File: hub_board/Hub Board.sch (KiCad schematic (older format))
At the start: 26 parts, among them J1 DotStar, J2 DotStar, J3 DotStar, J4 DotStar, J5 Sensor, P4 SERIAL, SW1 Switch_SPDT_x2, SW2 Switch_DPST, U0 10118194, U1 LM3671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

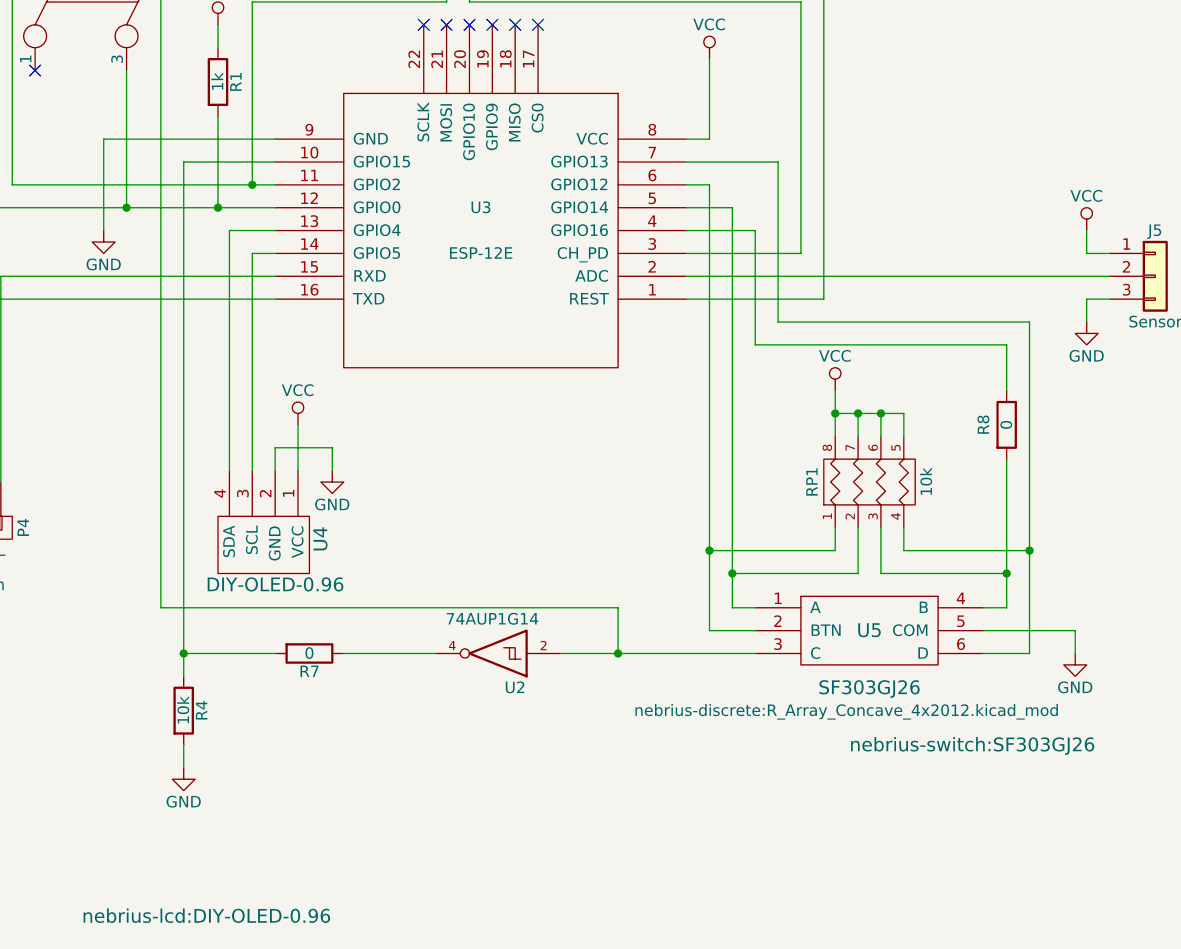
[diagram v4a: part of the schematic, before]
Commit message: Removed jumpers
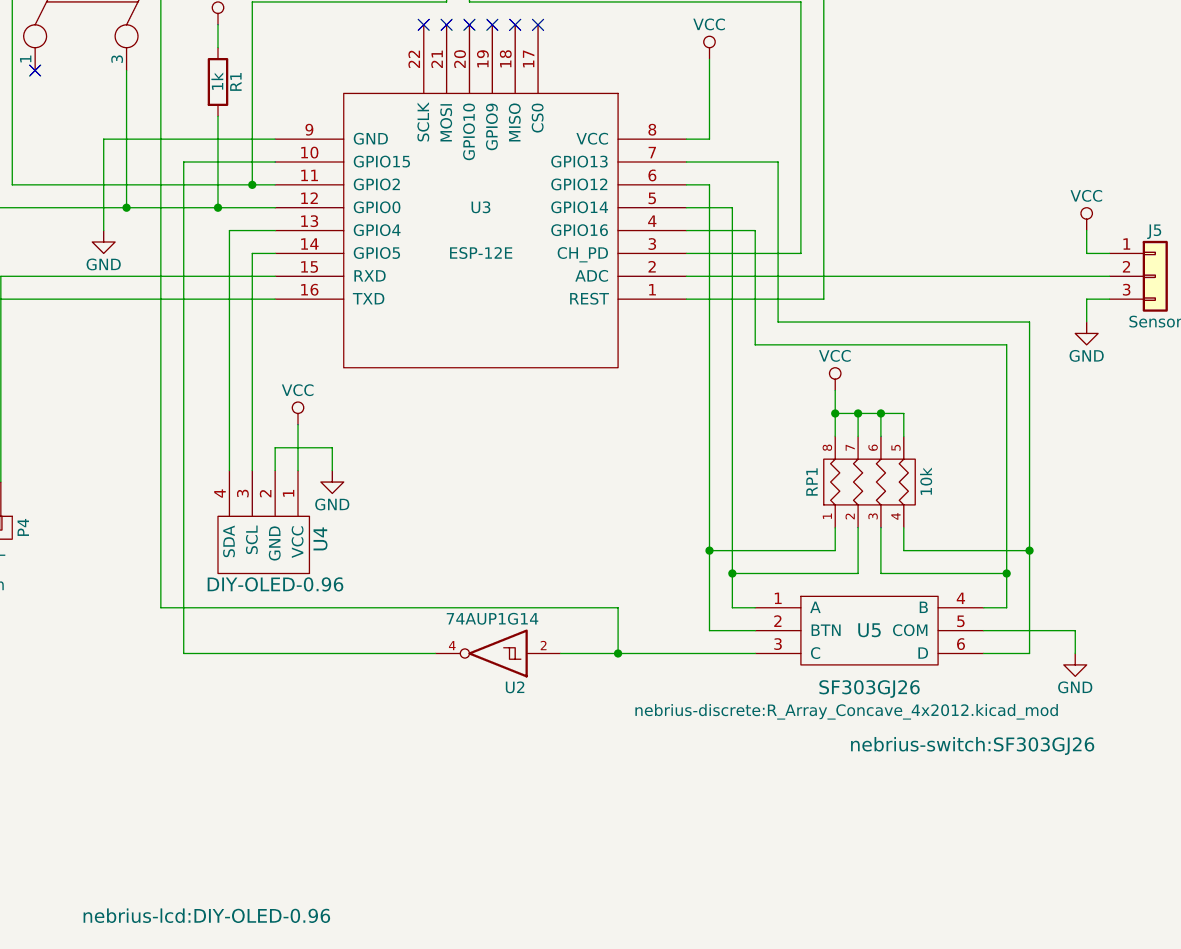
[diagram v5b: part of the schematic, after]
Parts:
- removed R4: 10k, Resistors_SMD:R_0805_HandSoldering, symbol R
- removed R7, R8: 0, Resistors_SMD:R_0805_HandSoldering, symbol R
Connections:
- net at U3.10 (GPIO15): now also U2.4
- net at U3.4 (GPIO16): now also RP1.3 (P3), U5.4 (B)
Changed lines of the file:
@@
 	9250 6400 9250 6500
-Wire Wire Line
-	5350 4350 5350 6600
 Wire Wire Line
 	7250 6300 7250 6500
@@
 	-1   0    0    1
 $EndComp
-$Comp
-L R R4
-U 1 1 5AB19A67
-P 5350 6750
-F 0 "R4" V 5430 6750 50  0000 C CNN
-F 1 "10k" V 5350 6750 50  0000 C CNN
-F 2 "Resistors_SMD:R_0805_HandSoldering" V 5280 6750 50  0001 C CNN
-F 3 "" H 5350 6750 50  0001 C CNN
-	1    5350 6750
-	1    0    0    -1
-$EndComp
-$Comp
-L R R7
-U 1 1 5AB19B14
-P 5900 6500
-F 0 "R7" V 5980 6500 50  0000 C CNN
-F 1 "0" V 5900 6500 50  0000 C CNN
-F 2 "Resistors_SMD:R_0805_HandSoldering" V 5830 6500 50  0001 C CNN
-F 3 "" H 5900 6500 50  0001 C CNN
-	1    5900 6500
-	0    1    1    0
-$EndComp
-Wire Wire Line
-	6450 6500 6050 6500
-Wire Wire Line
-	5350 6500 5750 6500
-Connection ~ 5350 6500
-$Comp
-L GND #PWR015
-U 1 1 5AB19DEB
-P 5350 7000
-F 0 "#PWR015" H 5350 6750 50  0001 C CNN
-F 1 "GND" H 5350 6850 50  0000 C CNN
-F 2 "" H 5350 7000 50  0001 C CNN
-F 3 "" H 5350 7000 50  0001 C CNN
-	1    5350 7000
-	1    0    0    -1
-$EndComp
-Wire Wire Line
-	5350 6900 5350 7000
 Wire Wire Line
 	7650 4450 7550 4450
@@
 Wire Wire Line
 	7650 4450 7650 6400
-$Comp
-L R R8
-U 1 1 5AB1A481
-P 8950 5500
-F 0 "R8" V 8850 5500 50  0000 C CNN
-F 1 "0" V 8950 5500 50  0000 C CNN
-F 2 "Resistors_SMD:R_0805_HandSoldering" V 8880 5500 50  0001 C CNN
-F 3 "" H 8950 5500 50  0001 C CNN
-	1    8950 5500
-	1    0    0    -1
-$EndComp
-Wire Wire Line
-	8950 5150 8950 5350
-Wire Wire Line
-	8950 5650 8950 6300
 $Comp
 L VCC #PWR016
@@
 Wire Wire Line
 	5250 6300 7250 6300
+Wire Wire Line
+	5350 4350 5350 6500
+Wire Wire Line
+	5350 6500 6450 6500
+Wire Wire Line
+	8950 5150 8950 6300
 $EndSCHEMATC

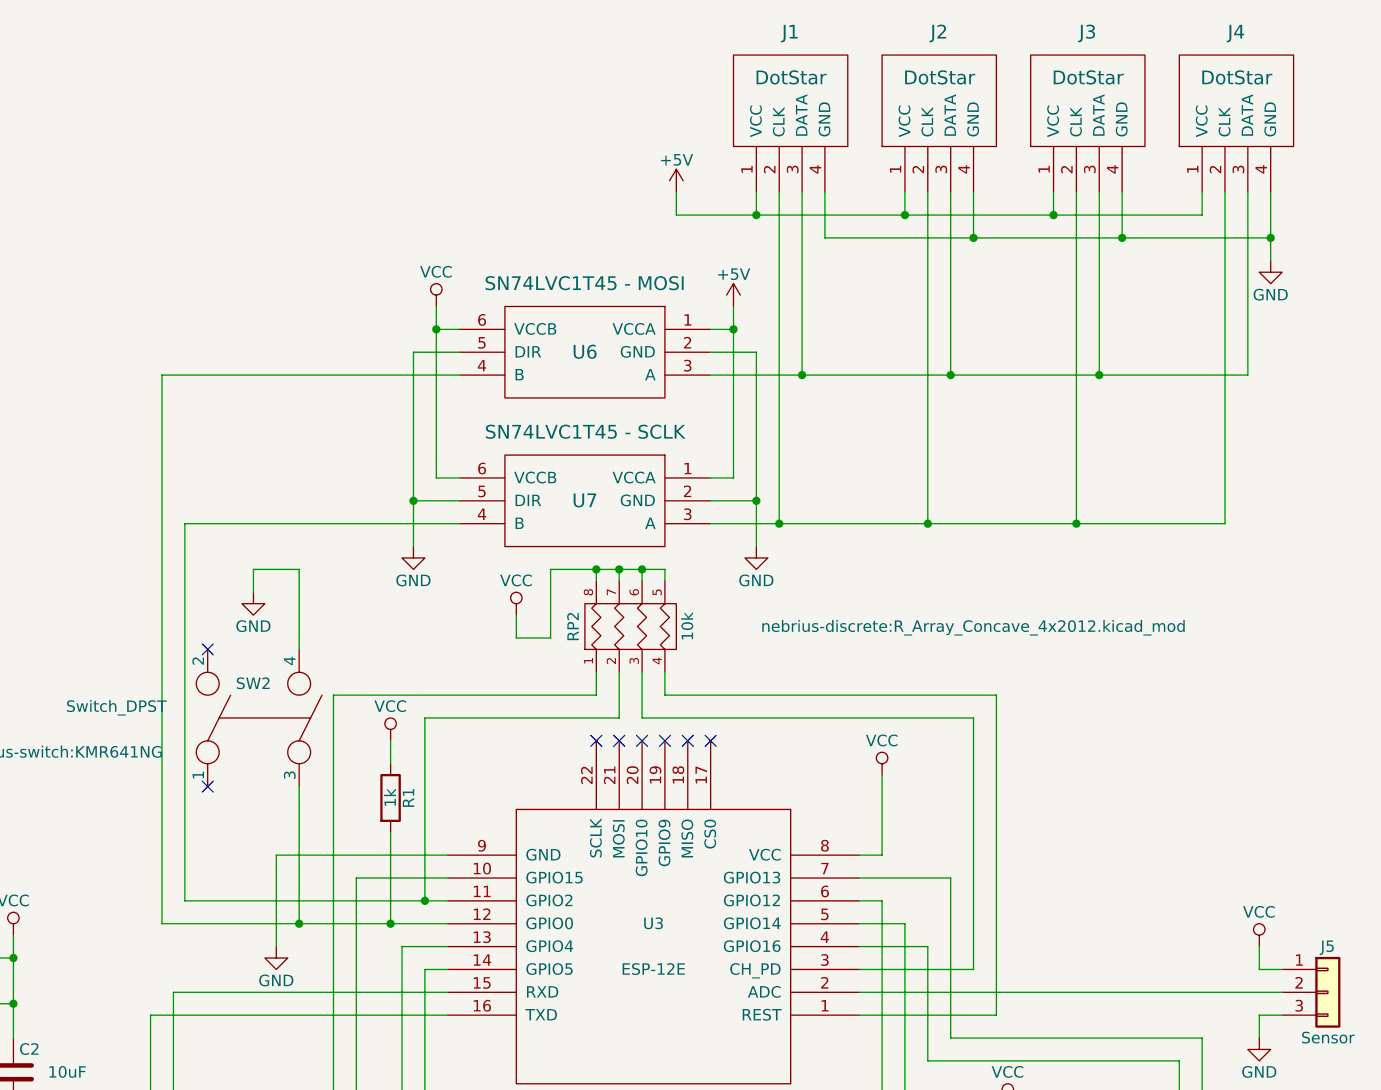
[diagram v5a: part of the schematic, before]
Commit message: Switched to using NeoPixels and other board cleanup
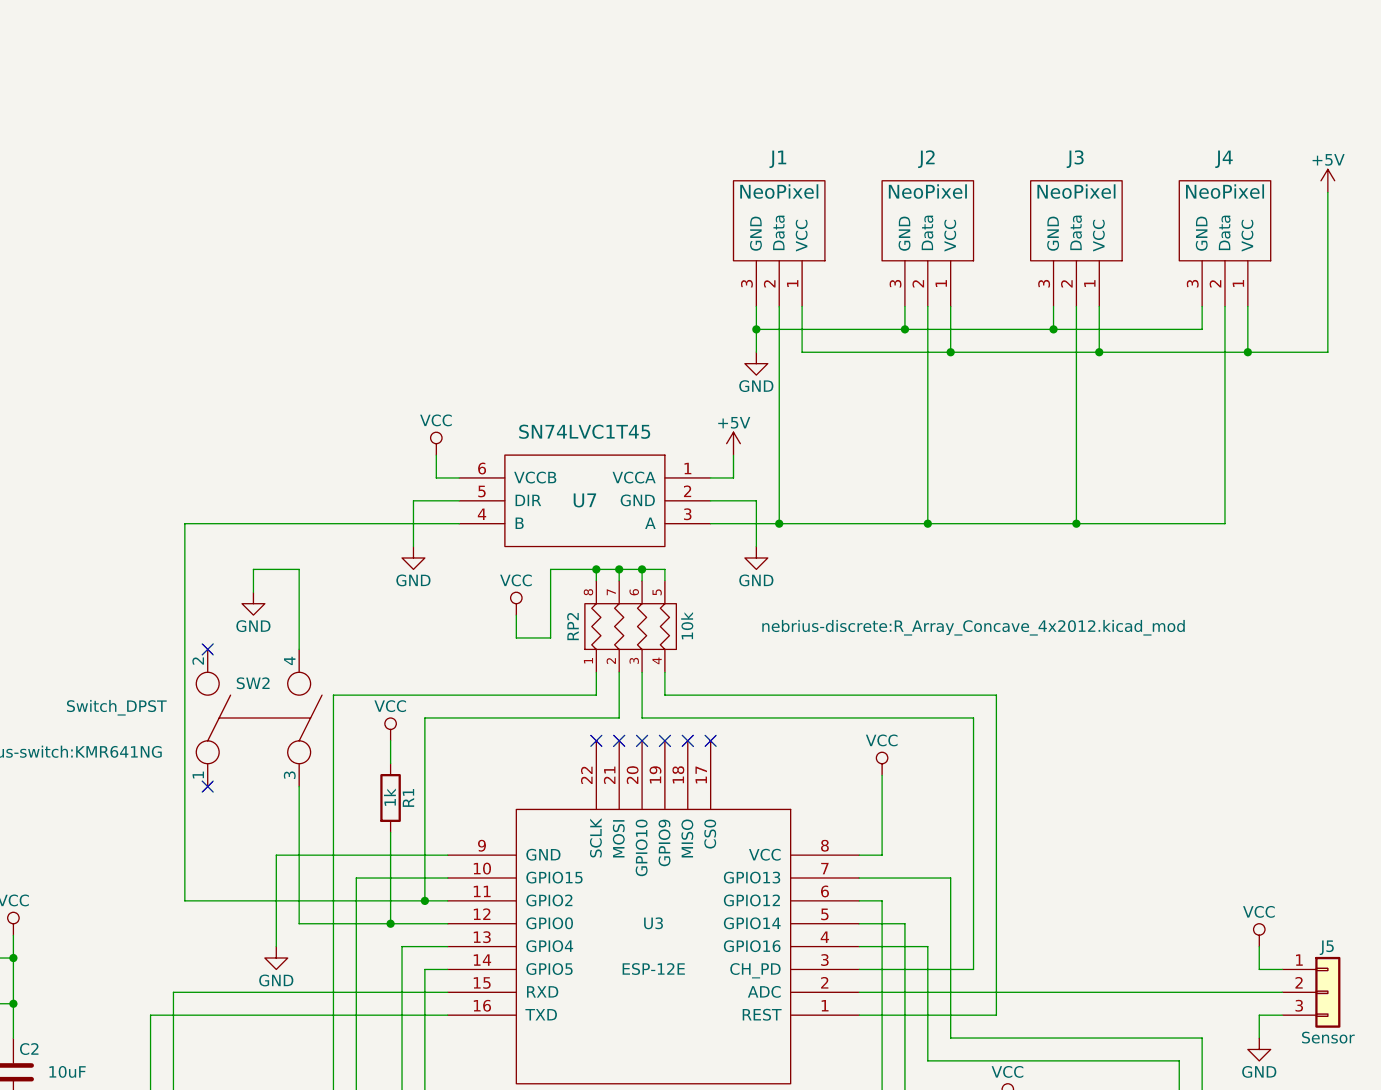
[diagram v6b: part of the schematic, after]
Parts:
- removed J1, J2, J3, J4: DotStar, Pin_Headers:Pin_Header_Angled_1x04_Pitch2.54mm, symbol DotStar
- removed U6: SN74LVC1T45 - MOSI, TO_SOT_Packages_SMD:SOT-23-6_Handsoldering, symbol SN74LVC1T45
- added J1, J2, J3, J4: NeoPixel, Pin_Headers:Pin_Header_Angled_1x03_Pitch2.54mm, symbol NeoPixel
- U7: value SN74LVC1T45 - SCLK -> SN74LVC1T45
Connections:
- net +5V: now also J1.1 (VCC), J2.1 (VCC), J3.1 (VCC), J4.1 (VCC)
- net GND: now also J1.3 (GND), J2.3 (GND), J3.3 (GND), J4.3 (GND)
- net at U7.3 (A): now also J1.2 (Data), J2.2 (Data), J3.2 (Data), J4.2 (Data)
